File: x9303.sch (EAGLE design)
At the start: 158 parts, among them CN11 ERC12864-2, CN12 SD-CARD_10P, IC1 7805DT, IC2 L1117, IC3 Pololu, IC4 MCP1700T30, J3 ERASE, K1 TP-1, K2 TP-1, K3 TP-1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

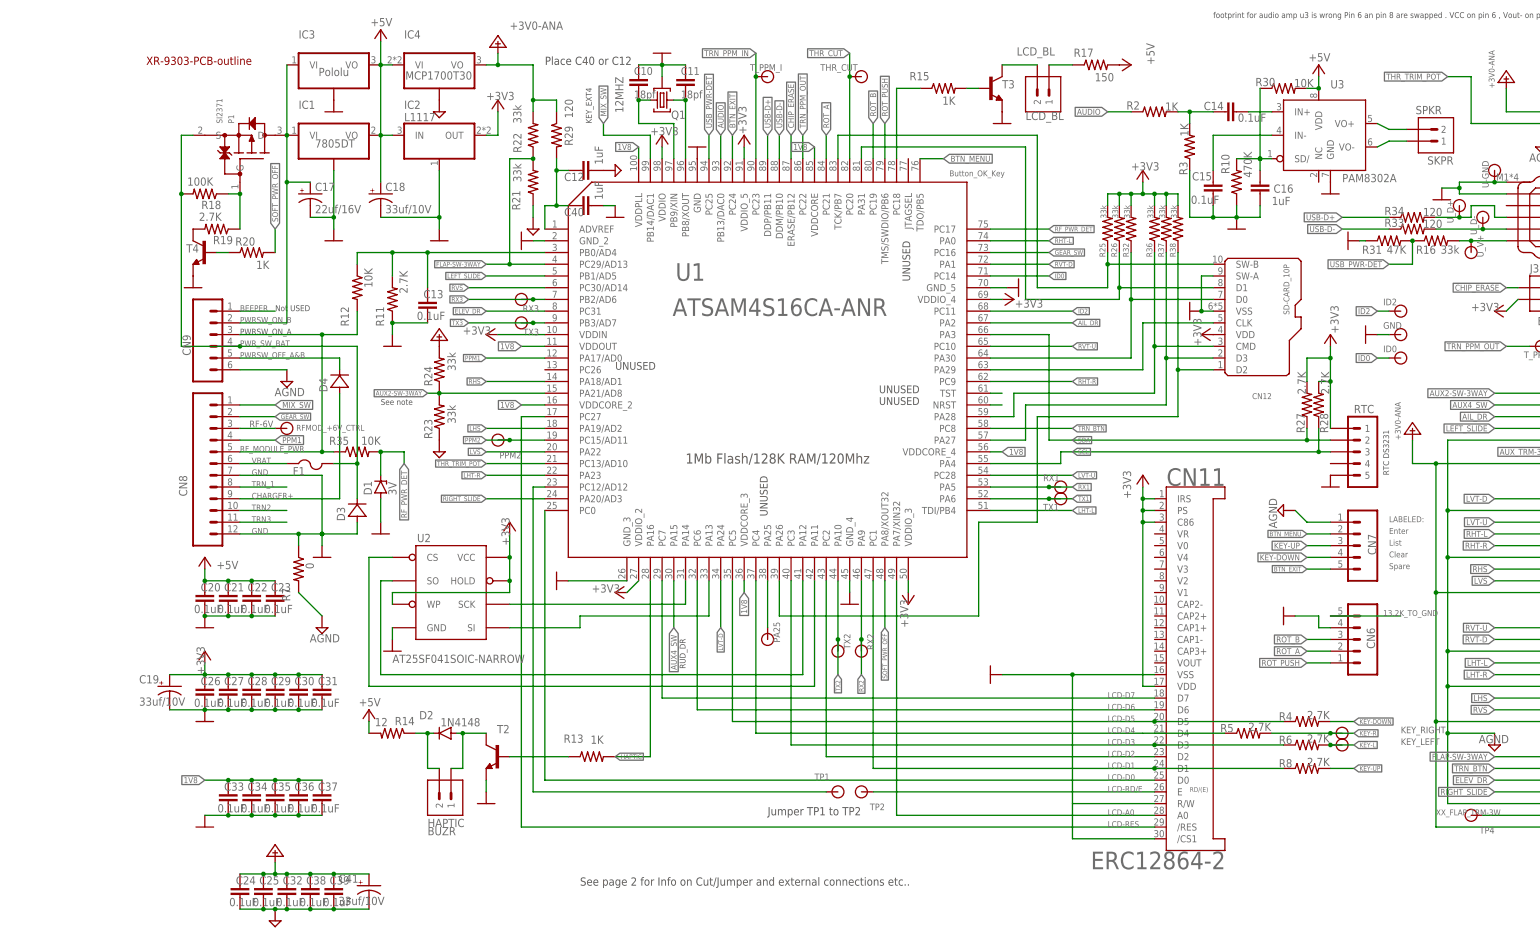
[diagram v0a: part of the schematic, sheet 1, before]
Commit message: added pictures and docs added firmware binary added old JR9303 wiring and pin-out doc added lcd display adapter patch boards for different displays
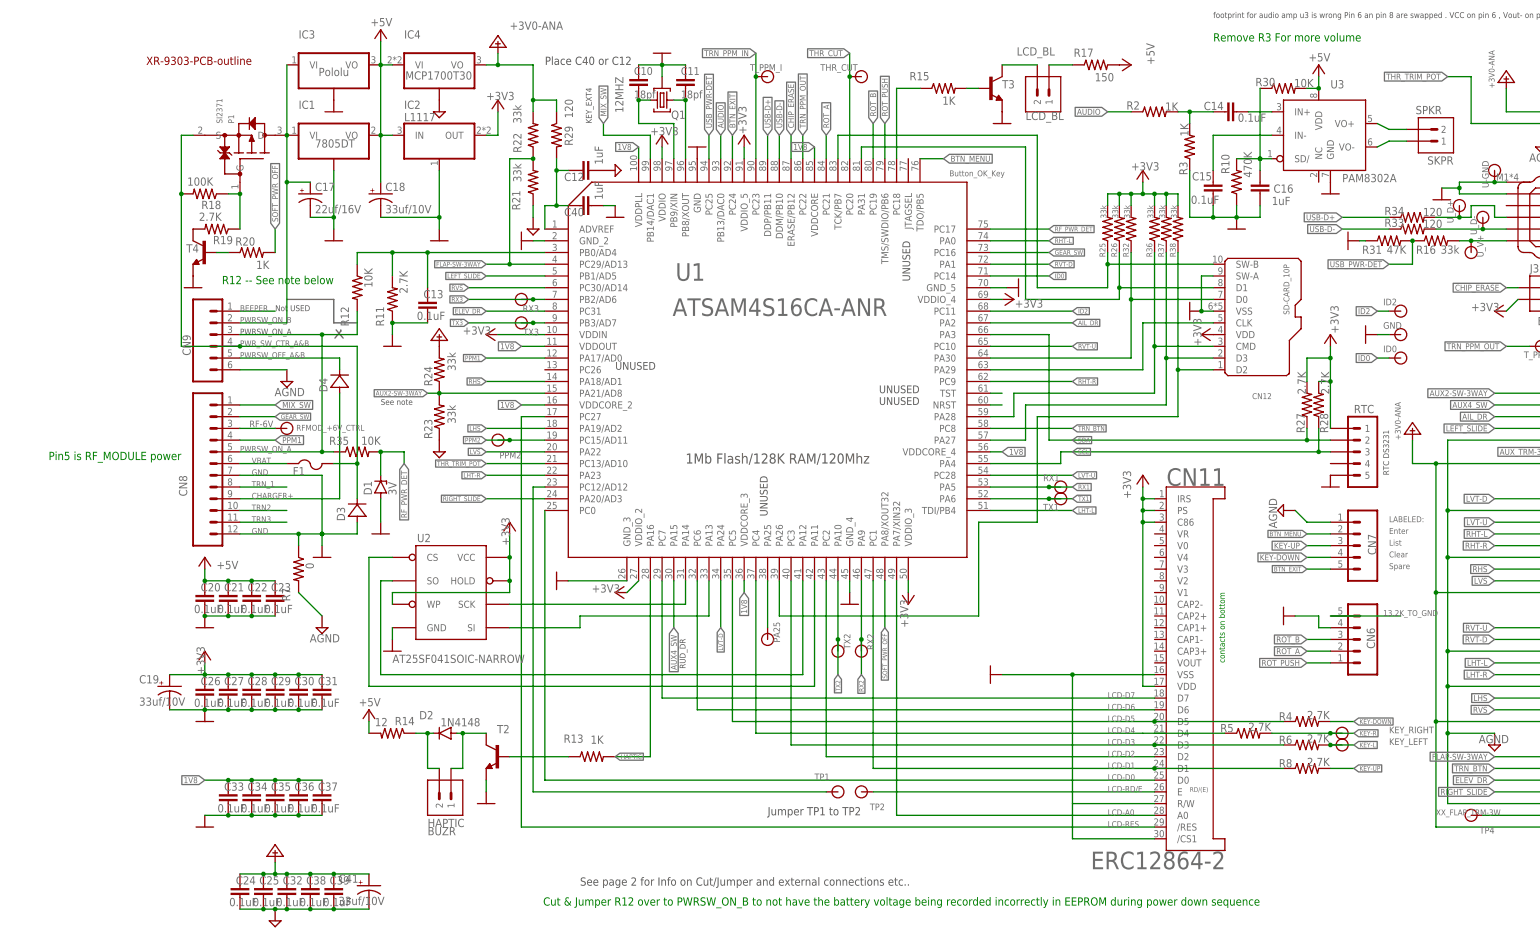
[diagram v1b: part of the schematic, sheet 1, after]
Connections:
- net PWR_SW_BAT renamed PWR_SW_CTR_A&B
- net RF_MODULE_PWR renamed PWRSW_ON_A
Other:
- note added: "Connect RX2 to signal labeled RF6V from RF bay - needed for MultiModul telemetry. Also make path for signal on RF bay"
- note added: "Cut & Jumper R12 over to PWRSW_ON_B to not have the battery voltage being recorded incorrectly in EEPROM during power down sequence"
- note added: "Explanation:Recorded the pin numbers incorrectrly for the horizontal Connectors AND Library elements for JST-N_PTH_VERT are opposite of what JR used. Therefore the two mistakes neutralized thenselves on the horizontal connectors but not on the vertical ones ."
- note added: "Pin5 is RF_MODULE power"
- note added: "R12 -- See note below"
- note added: "Remove R3 For more volume"
- note added: "The 4 required nav buttons are Menu/Ent, up, down. Left and right is not strictly needed if rotary encoder is present."
- note added: "contacts on bottom"
- note removed: "Explenation:Recorded the pin numbers incorrectrly for the horizontal Connectors AND Library elements for JST-N_PTH_VERT are opposite of what JR used. Therefore the two mistakes neutralized thenselves on the horizontal connectors but not on the vertical ones ."
- note removed: "The 4 required nav buttons are Menu/Ent, up, down. Left and right is not needed if rotary encoder is present."
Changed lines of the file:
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@@
 <text x="309.88" y="71.12" size="1.27" layer="97">CN1 pin 2 : use for ID2 connection to 3 way switch Aux2</text>
 <text x="81.28" y="-10.16" size="1.778" layer="97">See page 2 for Info on Cut/Jumper and external connections etc..</text>
+<text x="220.98" y="38.1" size="1.27" layer="91" rot="R90">contacts on bottom</text>
+<text x="228.6" y="-12.7" size="1.778" layer="91" rot="R180">Cut &amp; Jumper R12 over to PWRSW_ON_B to not have the battery voltage being recorded incorrectly in EEPROM during power down sequence</text>
+<text x="27.94" y="121.92" size="1.778" layer="91" rot="R180">R12 -- See note below</text>
+<text x="-5.08" y="83.82" size="1.778" layer="91" rot="R180">Pin5 is RF_MODULE power</text>
+<wire x1="33.02" y1="111.76" x2="27.94" y2="111.76" width="0.1524" layer="97"/>
+<wire x1="27.94" y1="111.76" x2="27.94" y2="116.84" width="0.1524" layer="97"/>
+<wire x1="27.94" y1="116.84" x2="17.78" y2="116.84" width="0.1524" layer="97"/>
+<wire x1="28.448" y1="110.236" x2="29.972" y2="108.458" width="0.1524" layer="97"/>
+<wire x1="28.194" y1="108.458" x2="29.464" y2="109.982" width="0.1524" layer="97"/>
+<wire x1="29.464" y1="109.982" x2="29.464" y2="110.236" width="0.1524" layer="97"/>
+<text x="218.44" y="172.72" size="1.778" layer="91">Remove R3 For more volume</text>
 </plain>
 <instances>
@@
 </instance>
 <instance part="KEY_RIGHT" gate="G$1" x="246.38" y="22.86" smashed="yes">
-<attribute name="NAME" x="259.08" y="22.86" size="1.4224" layer="95"/>
+<attribute name="NAME" x="256.54" y="22.86" size="1.4224" layer="95"/>
 </instance>
 <instance part="KEY_LEFT" gate="G$1" x="246.38" y="20.32" smashed="yes">
-<attribute name="NAME" x="259.08" y="20.32" size="1.4224" layer="95"/>
+<attribute name="NAME" x="256.54" y="20.32" size="1.4224" layer="95"/>
 </instance>
 <instance part="RF-6V" gate="G$1" x="17.78" y="88.9" smashed="yes">
@@
 </segment>
 </net>
-<net name="PWR_SW_BAT" class="0">
+<net name="PWR_SW_CTR_A&amp;B" class="0">
 <segment>
 <pinref part="CN9" gate="G$1" pin="4"/>
@@
 </segment>
 </net>
-<net name="RF_MODULE_PWR" class="0">
+<net name="PWRSW_ON_A" class="0">
 <segment>
 <pinref part="CN9" gate="G$1" pin="3"/>
@@
 <text x="-30.48" y="25.4" size="1.27" layer="97">Adjust R23,R24 so that current consumption reading roughly corresponds to actual consumption -- Or ad circuitry INA138 -- disconnect trace from CN4 pin1</text>
 <text x="-30.48" y="50.8" size="1.27" layer="97">Need to install CN6,7,8 &amp; 9 (vertical ones) 180 deg. turned so that pin 1 becomes pin-N. or install on the back of the PCB for the same reason. </text>
-<text x="-30.48" y="45.72" size="1.27" layer="97">Explenation:Recorded the pin numbers incorrectrly for the horizontal Connectors AND Library elements for JST-N_PTH_VERT are opposite of what JR used.
+<text x="-30.48" y="45.72" size="1.27" layer="97">Explanation:Recorded the pin numbers incorrectrly for the horizontal Connectors AND Library elements for JST-N_PTH_VERT are opposite of what JR used.
 Therefore the two mistakes neutralized thenselves on the horizontal connectors but not on the vertical ones .</text>
 <text x="109.22" y="53.34" size="1.016" layer="96">TRN_BTN needs to be normally closed </text>
@@
 <text x="109.22" y="43.18" size="1.27" layer="97">PPM1 is referred to as "External" in Firmware</text>
 <text x="109.22" y="40.64" size="1.27" layer="97">PPM2 is referred to as Internal in FW</text>
-<text x="109.22" y="38.1" size="1.27" layer="97">The 4 required nav buttons are Menu/Ent, up, down. Left and right is not needed if rotary encoder is present.</text>
+<text x="109.22" y="38.1" size="1.27" layer="97">The 4 required nav buttons are Menu/Ent, up, down. Left and right is not strictly  needed if rotary encoder is present.</text>
+<text x="-30.48" y="17.78" size="1.27" layer="150">Connect RX2 to signal labeled RF6V from RF bay - needed for MultiModul telemetry. Also make path for signal on RF bay</text>
 </plain>
 <instances>
